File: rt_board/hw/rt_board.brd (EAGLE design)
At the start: 100 x 80 mm, 65 parts, among them IC1 MCP170333MB, IC2/L1 TLE4935L, IC3/L1 TLE4935L, IC4/L1 TLE4935L, IC5/L1 TLE4935L, Q1 8MHz, SW1 B3U-1000PM-B, SW2 B3U-1000PM-B, U1 DRV8801PWP, U2 DRV8801PWP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

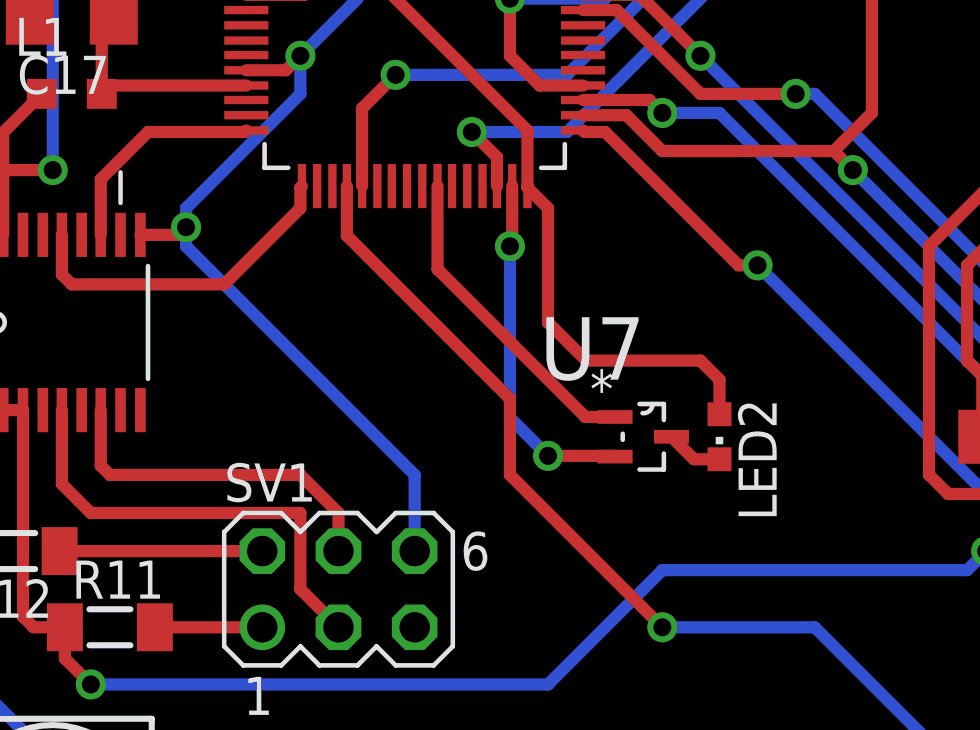
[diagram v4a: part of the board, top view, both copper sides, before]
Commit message: fixed and simplified user-defined LED-1 control
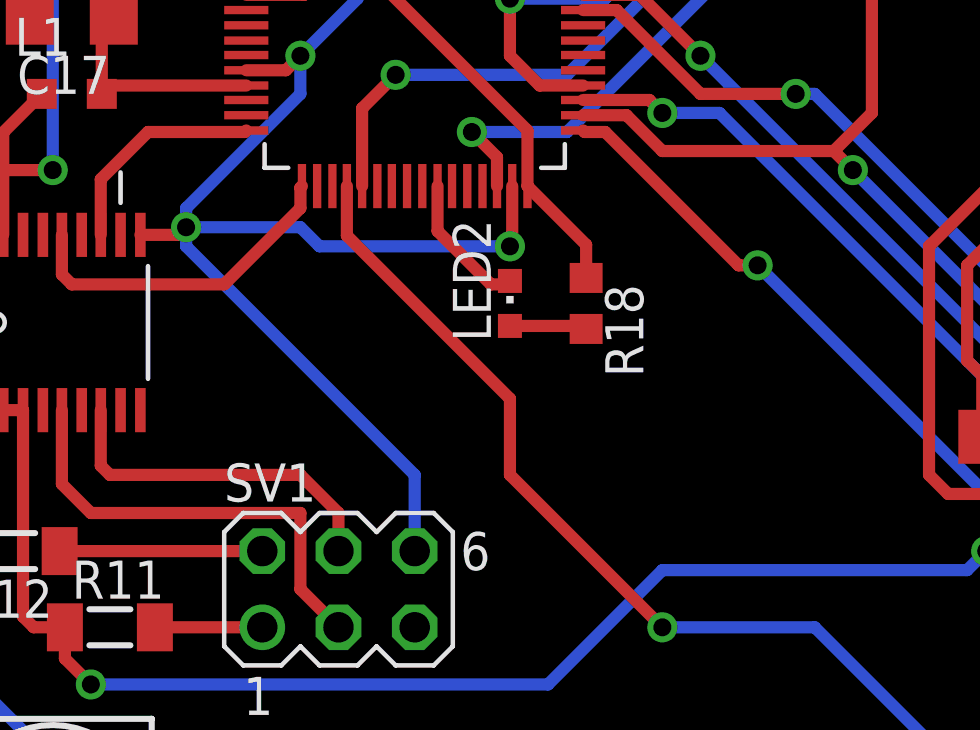
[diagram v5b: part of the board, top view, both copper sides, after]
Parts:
- removed U7: 2N7002BKW, 2n7002:SOT65P210X110-3N
- added R18: 240R, rcl:R0603
- moved LED2 8.28 mm to (36.2, 31.1), turned to 0 degrees
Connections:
- removed net N$47: LED2.C, U7.3
- new net N$1: LED2.C, U6.26
- net +5V: now also R18.1; no longer LED2.A
- net 0V: no longer U7.2
- net N$44: now also LED2.A, R18.2; no longer U6.26, U7.1
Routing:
- net +5V: track 118.5 -> 109.9 mm
- net N$44: track 10.7 -> 2.58 mm
- net N$1: track 0.00 -> 4.70 mm
- net N$47: track 1.91 -> 0.00 mm
- net 0V: track 80.0 -> 81.3 mm, vias 14 -> 13
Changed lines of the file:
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@@
 <element name="LED1" library="led" package="CHIPLED_0603" value="GREEN" x="20.32" y="62.23" rot="R180"/>
 <element name="R17" library="rcl" package="R0603" value="470R" x="23.495" y="62.23" rot="R90"/>
-<element name="U7" library="2n7002" package="SOT65P210X110-3N" value="2N7002BKW" x="40.64" y="26.67">
-<attribute name="PACKAGE" value="SOT-3" x="40.64" y="26.67" size="1.778" layer="27" display="off"/>
-<attribute name="OC_NEWARK" value="55T7739" x="40.64" y="26.67" size="1.778" layer="27" display="off"/>
-<attribute name="MPN" value="2N7002BKW" x="40.64" y="26.67" size="1.778" layer="27" display="off"/>
-<attribute name="SUPPLIER" value="NXP Semiconductors" x="40.64" y="26.67" size="1.778" layer="27" display="off"/>
-<attribute name="OC_FARNELL" value="1894713" x="40.64" y="26.67" size="1.778" layer="27" display="off"/>
-</element>
-<element name="LED2" library="led" package="CHIPLED_0603" value="GREEN" x="43.18" y="26.67" rot="R180"/>
+<element name="LED2" library="led" package="CHIPLED_0603" value="GREEN" x="36.195" y="31.115"/>
 <element name="SW1" library="basz" package="SPST-NO" value="B3U-1000PM-B" x="27.94" y="50.8"/>
 <element name="SW2" library="basz" package="SPST-NO" value="B3U-1000PM-B" x="21.59" y="50.8"/>
+<element name="R18" library="rcl" package="R0603" value="240R" x="38.735" y="31.115" rot="R270"/>
 </elements>
 <signals>
@@
 <contactref element="U2" pad="16"/>
 <contactref element="LED1" pad="C"/>
-<contactref element="U7" pad="2"/>
 <contactref element="SW2" pad="P$1"/>
 <polygon width="0.4064" layer="1">
@@
 <vertex x="73.66" y="78.74"/>
 </polygon>
-<wire x1="36.2712" y1="35.0266" x2="36.2712" y2="33.0962" width="0.4064" layer="1"/>
-<wire x1="36.2712" y1="33.0962" x2="36.195" y2="33.02" width="0.4064" layer="1"/>
-<via x="36.195" y="33.02" extent="1-16" drill="0.6"/>
-<wire x1="36.195" y1="33.02" x2="36.195" y2="27.305" width="0.4064" layer="16"/>
-<wire x1="36.195" y1="27.305" x2="37.465" y2="26.035" width="0.4064" layer="16"/>
-<via x="37.465" y="26.035" extent="1-16" drill="0.6"/>
-<wire x1="37.465" y1="26.035" x2="39.6748" y2="26.035" width="0.4064" layer="1"/>
-<wire x1="39.6748" y1="26.035" x2="39.7002" y2="26.0096" width="0.4064" layer="1"/>
 <wire x1="23.876" y1="33.401" x2="25.146" y2="33.401" width="0.4064" layer="1"/>
 <wire x1="25.146" y1="33.401" x2="25.4" y2="33.655" width="0.4064" layer="1"/>
@@
 <via x="47.625" y="9.525" extent="1-16" drill="2.8"/>
 <via x="57.785" y="76.835" extent="1-16" drill="2.8"/>
+<wire x1="36.2712" y1="35.0266" x2="36.2712" y2="33.0962" width="0.4064" layer="1"/>
+<wire x1="36.2712" y1="33.0962" x2="36.195" y2="33.02" width="0.4064" layer="1"/>
+<via x="36.195" y="33.02" extent="1-16" drill="0.6"/>
+<wire x1="36.195" y1="33.02" x2="29.845" y2="33.02" width="0.4064" layer="16"/>
+<wire x1="29.845" y1="33.02" x2="29.21" y2="33.655" width="0.4064" layer="16"/>
+<wire x1="29.21" y1="33.655" x2="25.4" y2="33.655" width="0.4064" layer="16"/>
 </signal>
 <signal name="+5V">
@@
 <contactref element="U3" pad="16"/>
 <contactref element="R17" pad="1"/>
-<contactref element="LED2" pad="A"/>
 <contactref element="SW1" pad="P$2"/>
 <wire x1="33.02" y1="53.34" x2="31.98" y2="53.34" width="0.4064" layer="1"/>
@@
 <wire x1="24.13" y1="54.61" x2="27.305" y2="57.785" width="0.4064" layer="1"/>
 <wire x1="27.305" y1="57.785" x2="27.305" y2="61.465" width="0.4064" layer="1"/>
-<wire x1="43.18" y1="27.42" x2="43.18" y2="28.575" width="0.4064" layer="1"/>
-<wire x1="43.18" y1="28.575" x2="42.545" y2="29.21" width="0.4064" layer="1"/>
-<wire x1="42.545" y1="29.21" x2="38.735" y2="29.21" width="0.4064" layer="1"/>
-<wire x1="38.735" y1="29.21" x2="37.465" y2="30.48" width="0.4064" layer="1"/>
-<wire x1="36.7792" y1="35.0266" x2="36.7792" y2="34.9758" width="0.4064" layer="1"/>
-<wire x1="36.7792" y1="34.9758" x2="37.465" y2="34.29" width="0.4064" layer="1"/>
-<wire x1="37.465" y1="34.29" x2="37.465" y2="30.48" width="0.4064" layer="1"/>
 <wire x1="27.4066" y1="44.3992" x2="29.2608" y2="44.3992" width="0.4064" layer="1"/>
 <wire x1="36.7792" y1="35.0266" x2="36.7792" y2="36.8808" width="0.4064" layer="1"/>
@@
 <wire x1="15.24" y1="59.795" x2="21.91" y2="59.795" width="0.4064" layer="1"/>
 <wire x1="21.91" y1="59.795" x2="23.495" y2="61.38" width="0.4064" layer="1"/>
+<contactref element="R18" pad="1"/>
+<wire x1="38.735" y1="31.965" x2="38.735" y2="33.0708" width="0.4064" layer="1"/>
+<wire x1="38.735" y1="33.0708" x2="36.7792" y2="35.0266" width="0.4064" layer="1"/>
 </signal>
 <signal name="+12V">
@@
 <wire x1="20.32" y1="63.08" x2="20.32" y2="62.98" width="0.4064" layer="1"/>
 </signal>
-<signal name="N$44">
-<contactref element="U6" pad="26"/>
-<contactref element="U7" pad="1"/>
-<wire x1="33.782" y1="35.0266" x2="33.782" y2="32.258" width="0.4064" layer="1"/>
-<wire x1="33.782" y1="32.258" x2="38.7096" y2="27.3304" width="0.4064" layer="1"/>
-<wire x1="39.7002" y1="27.3304" x2="38.7096" y2="27.3304" width="0.4064" layer="1"/>
-</signal>
-<signal name="N$47">
-<contactref element="U7" pad="3"/>
-<contactref element="LED2" pad="C"/>
-<wire x1="43.18" y1="25.92" x2="42.3298" y2="25.92" width="0.4064" layer="1"/>
-<wire x1="42.3298" y1="25.92" x2="41.5798" y2="26.67" width="0.4064" layer="1"/>
-</signal>
 <signal name="N$50">
 <polygon width="0.4064" layer="16">
@@
 </polygon>
 </signal>
+<signal name="N$1">
+<contactref element="U6" pad="26"/>
+<contactref element="LED2" pad="C"/>
+<wire x1="33.782" y1="35.0266" x2="33.782" y2="33.528" width="0.4064" layer="1"/>
+<wire x1="33.782" y1="33.528" x2="35.56" y2="31.75" width="0.4064" layer="1"/>
+<wire x1="35.56" y1="31.75" x2="36.08" y2="31.75" width="0.4064" layer="1"/>
+<wire x1="36.08" y1="31.75" x2="36.195" y2="31.865" width="0.4064" layer="1"/>
+</signal>
+<signal name="N$44">
+<contactref element="LED2" pad="A"/>
+<contactref element="R18" pad="2"/>
+<wire x1="36.195" y1="30.365" x2="38.635" y2="30.365" width="0.4064" layer="1"/>
+<wire x1="38.635" y1="30.365" x2="38.735" y2="30.265" width="0.4064" layer="1"/>
+</signal>
 </signals>

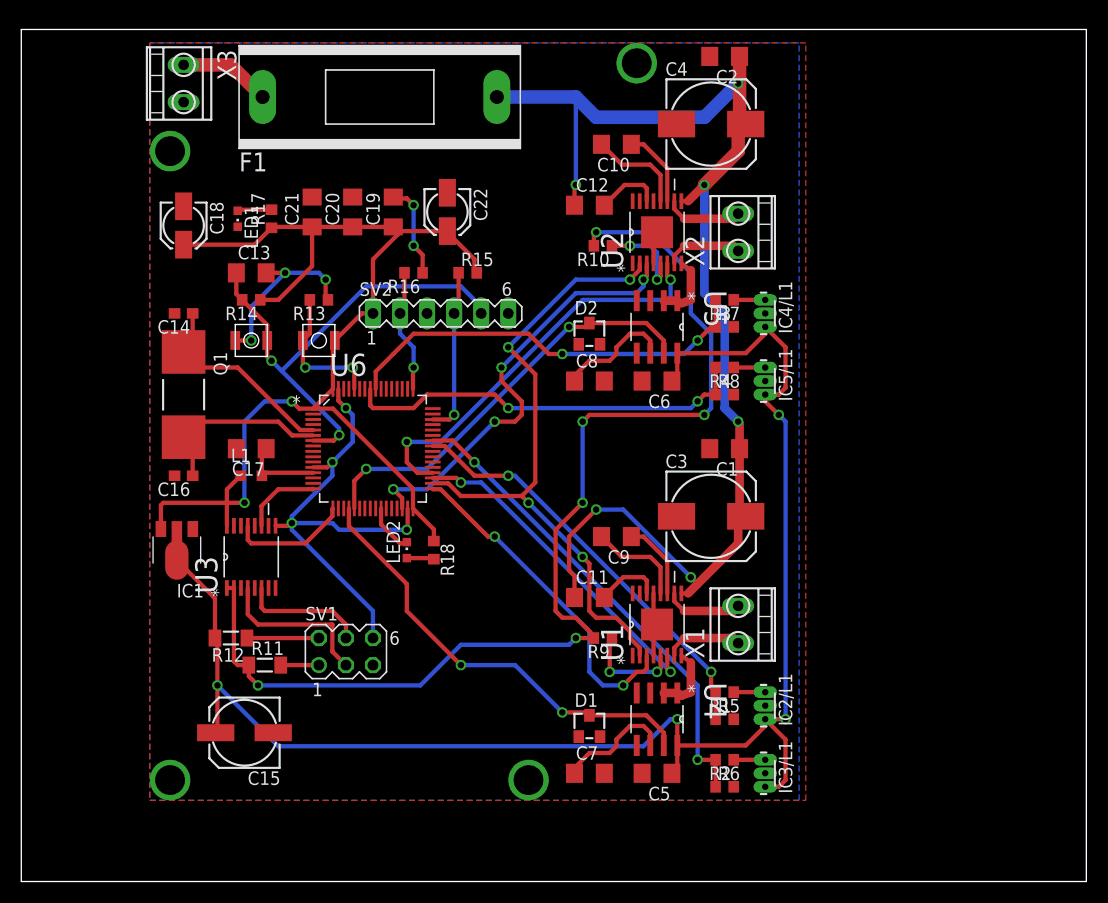
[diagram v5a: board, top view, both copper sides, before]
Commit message: added user LED 2
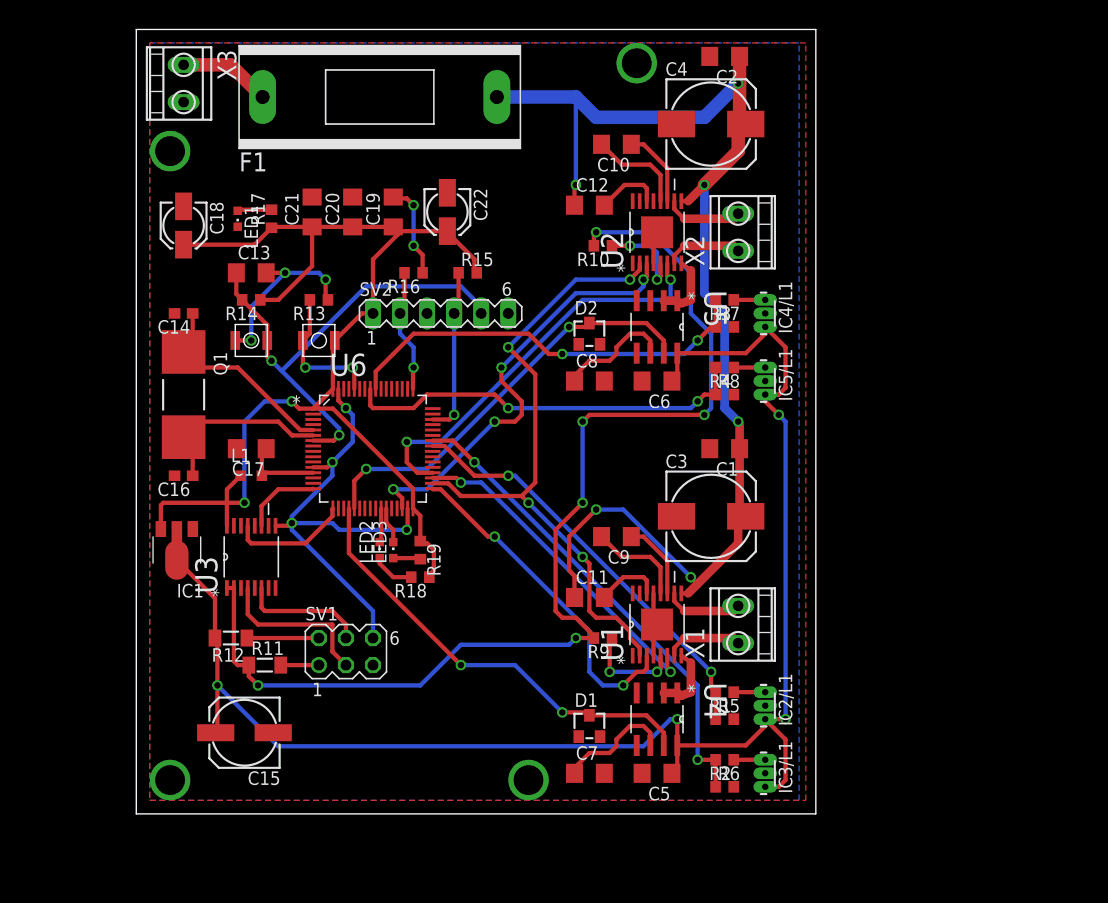
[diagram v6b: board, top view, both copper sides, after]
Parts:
- added LED3: GREEN, led:CHIPLED_0603
- added R19: 240R, rcl:R0603
- moved R18 2.84 mm to (37.5, 28.6), turned to 180 degrees
- moved LED2 2.54 mm to (33.7, 31.1)
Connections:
- new net N$47: LED3.C, U6.27
- new net N$51: LED3.A, R19.2
- net +5V: now also R19.1
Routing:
- net +5V: track 109.9 -> 113.7 mm
- net N$47: track 0.00 -> 3.44 mm
- net N$51: track 0.00 -> 2.58 mm
- net N$1: track 4.70 -> 3.21 mm
- net N$44: track 2.58 -> 4.01 mm
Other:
- board size 100 x 80 mm -> 63.8 x 73.7 mm
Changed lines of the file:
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@@
 <board>
 <plain>
-<wire x1="0" y1="0" x2="100" y2="0" width="0" layer="20"/>
-<wire x1="100" y1="0" x2="100" y2="80" width="0" layer="20"/>
-<wire x1="100" y1="80" x2="0" y2="80" width="0" layer="20"/>
-<wire x1="0" y1="80" x2="0" y2="0" width="0" layer="20"/>
+<wire x1="10.795" y1="6.35" x2="74.6" y2="6.35" width="0" layer="20"/>
+<wire x1="74.6" y1="6.35" x2="74.6" y2="80" width="0" layer="20"/>
+<wire x1="74.6" y1="80" x2="10.795" y2="80" width="0" layer="20"/>
+<wire x1="10.795" y1="80" x2="10.795" y2="6.35" width="0" layer="20"/>
 <text x="42.545" y="73.025" size="1.778" layer="26" rot="MR0">FASE FUSE 8A</text>
 <text x="16.51" y="71.755" size="1.778" layer="26" rot="MR90">+12V</text>
@@
 <element name="LED1" library="led" package="CHIPLED_0603" value="GREEN" x="20.32" y="62.23" rot="R180"/>
 <element name="R17" library="rcl" package="R0603" value="470R" x="23.495" y="62.23" rot="R90"/>
-<element name="LED2" library="led" package="CHIPLED_0603" value="GREEN" x="36.195" y="31.115"/>
+<element name="LED2" library="led" package="CHIPLED_0603" value="GREEN" x="33.655" y="31.115"/>
 <element name="SW1" library="basz" package="SPST-NO" value="B3U-1000PM-B" x="27.94" y="50.8"/>
 <element name="SW2" library="basz" package="SPST-NO" value="B3U-1000PM-B" x="21.59" y="50.8"/>
-<element name="R18" library="rcl" package="R0603" value="240R" x="38.735" y="31.115" rot="R270"/>
+<element name="R18" library="rcl" package="R0603" value="240R" x="37.465" y="28.575" rot="R180"/>
+<element name="LED3" library="led" package="CHIPLED_0603" value="GREEN" x="34.925" y="31.115"/>
+<element name="R19" library="rcl" package="R0603" value="240R" x="37.465" y="31.115" rot="R270"/>
 </elements>
 <signals>
@@
 <wire x1="21.91" y1="59.795" x2="23.495" y2="61.38" width="0.4064" layer="1"/>
 <contactref element="R18" pad="1"/>
-<wire x1="38.735" y1="31.965" x2="38.735" y2="33.0708" width="0.4064" layer="1"/>
-<wire x1="38.735" y1="33.0708" x2="36.7792" y2="35.0266" width="0.4064" layer="1"/>
+<contactref element="R19" pad="1"/>
+<wire x1="37.465" y1="34.3408" x2="36.7792" y2="35.0266" width="0.4064" layer="1"/>
+<wire x1="37.465" y1="31.965" x2="37.465" y2="34.3408" width="0.4064" layer="1"/>
+<wire x1="38.315" y1="28.575" x2="38.315" y2="28.79" width="0.4064" layer="1"/>
+<wire x1="38.315" y1="28.79" x2="38.735" y2="29.21" width="0.4064" layer="1"/>
+<wire x1="38.735" y1="29.21" x2="38.735" y2="31.115" width="0.4064" layer="1"/>
+<wire x1="38.735" y1="31.115" x2="38.1" y2="31.75" width="0.4064" layer="1"/>
+<wire x1="38.1" y1="31.75" x2="37.68" y2="31.75" width="0.4064" layer="1"/>
+<wire x1="37.68" y1="31.75" x2="37.465" y2="31.965" width="0.4064" layer="1"/>
 </signal>
 <signal name="+12V">
@@
 <wire x1="58.69" y1="15.605" x2="60.325" y2="13.97" width="0.4064" layer="1"/>
 <wire x1="60.325" y1="13.97" x2="60.325" y2="12.7762" width="0.4064" layer="1"/>
-<wire x1="30.7594" y1="35.0266" x2="30.7594" y2="33.3756" width="0.4064" layer="1"/>
-<wire x1="30.7594" y1="33.3756" x2="36.195" y2="27.94" width="0.4064" layer="1"/>
-<wire x1="36.195" y1="27.94" x2="36.195" y2="25.4" width="0.4064" layer="1"/>
-<wire x1="36.195" y1="25.4" x2="41.275" y2="20.32" width="0.4064" layer="1"/>
+<wire x1="30.7594" y1="35.0266" x2="30.7594" y2="30.8356" width="0.4064" layer="1"/>
+<wire x1="30.7594" y1="30.8356" x2="41.275" y2="20.32" width="0.4064" layer="1"/>
 <via x="41.275" y="20.32" extent="1-16" drill="0.6"/>
 <wire x1="41.275" y1="20.32" x2="46.355" y2="20.32" width="0.4064" layer="16"/>
@@
 <contactref element="U6" pad="26"/>
 <contactref element="LED2" pad="C"/>
-<wire x1="33.782" y1="35.0266" x2="33.782" y2="33.528" width="0.4064" layer="1"/>
-<wire x1="33.782" y1="33.528" x2="35.56" y2="31.75" width="0.4064" layer="1"/>
-<wire x1="35.56" y1="31.75" x2="36.08" y2="31.75" width="0.4064" layer="1"/>
-<wire x1="36.08" y1="31.75" x2="36.195" y2="31.865" width="0.4064" layer="1"/>
+<wire x1="33.782" y1="35.0266" x2="33.782" y2="31.992" width="0.4064" layer="1"/>
+<wire x1="33.782" y1="31.992" x2="33.655" y2="31.865" width="0.4064" layer="1"/>
 </signal>
 <signal name="N$44">
 <contactref element="LED2" pad="A"/>
 <contactref element="R18" pad="2"/>
-<wire x1="36.195" y1="30.365" x2="38.635" y2="30.365" width="0.4064" layer="1"/>
-<wire x1="38.635" y1="30.365" x2="38.735" y2="30.265" width="0.4064" layer="1"/>
+<wire x1="33.655" y1="30.365" x2="33.655" y2="29.845" width="0.4064" layer="1"/>
+<wire x1="33.655" y1="29.845" x2="34.925" y2="28.575" width="0.4064" layer="1"/>
+<wire x1="34.925" y1="28.575" x2="36.615" y2="28.575" width="0.4064" layer="1"/>
+</signal>
+<signal name="N$47">
+<contactref element="U6" pad="27"/>
+<contactref element="LED3" pad="C"/>
+<wire x1="34.2646" y1="35.0266" x2="34.2646" y2="33.6804" width="0.4064" layer="1"/>
+<wire x1="34.2646" y1="33.6804" x2="34.925" y2="33.02" width="0.4064" layer="1"/>
+<wire x1="34.925" y1="33.02" x2="34.925" y2="31.865" width="0.4064" layer="1"/>
+</signal>
+<signal name="N$51">
+<contactref element="LED3" pad="A"/>
+<contactref element="R19" pad="2"/>
+<wire x1="34.925" y1="30.365" x2="37.365" y2="30.365" width="0.4064" layer="1"/>
+<wire x1="37.365" y1="30.365" x2="37.465" y2="30.265" width="0.4064" layer="1"/>
 </signal>
 </signals>

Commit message: fixed layout of names and values of devices, so that it is readable
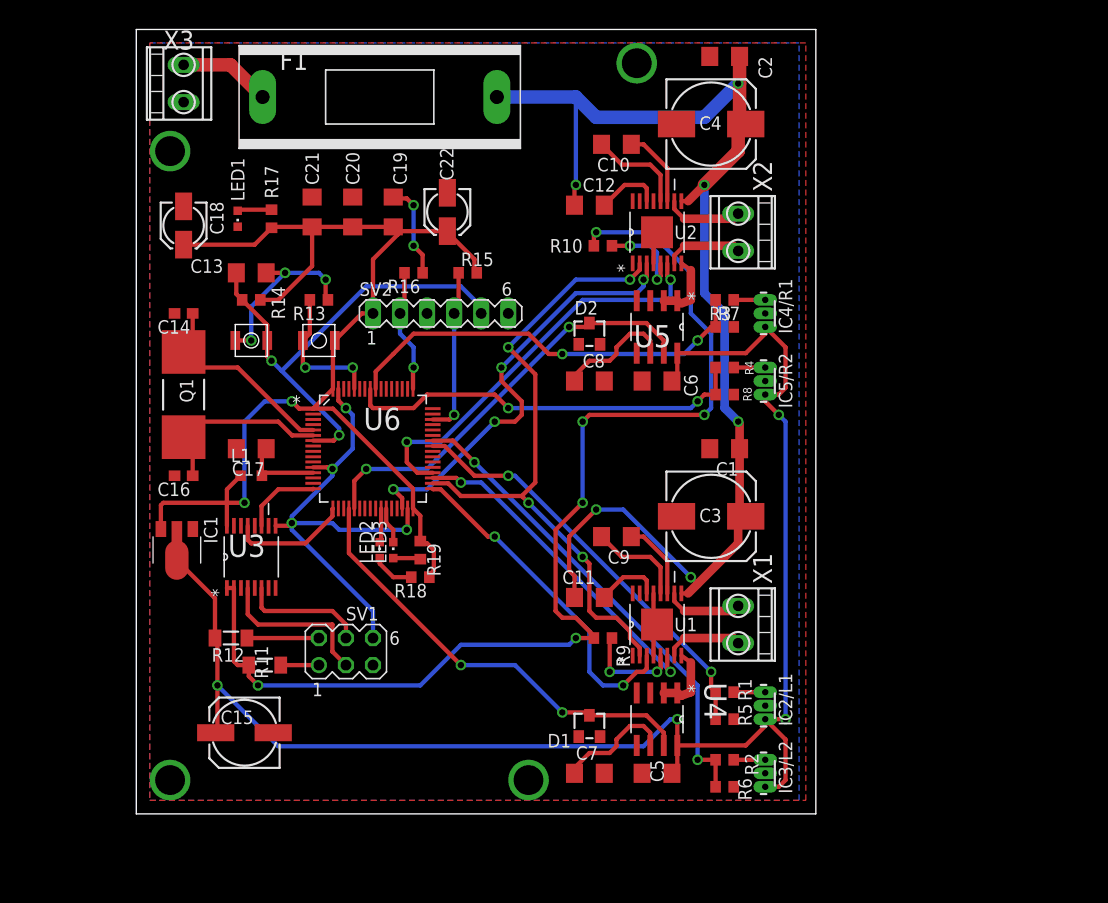
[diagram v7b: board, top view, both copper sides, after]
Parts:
- renumbered IC3/L1 to IC3/L2, IC4/L1 to IC4/R1, IC5/L1 to IC5/R2
